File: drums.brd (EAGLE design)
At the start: 212.1 x 294.3 mm, 210 parts, among them IC1 4051N, IC3 7812T, IC5 OPA2134P, IC6 OPA4130P, IC7 LM2574HVN-5.0, IC8 74LS595N, J2 UBBS-4R-D14-4D

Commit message: added hihats, buncha stuff
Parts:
- added C49, C52, C56, C57, C64, C65: 15n, dan:C050-025X075
- added C50, C51: 10n, dan:C050-025X075
- added C53, C54: 12n, dan:C050-025X075
- added C55: 3.3n, dan:C050-025X075
- added C58, C62: 1u, dan:E2-5
- added C59: np, dan:C050-025X075
- added C60: .47u, dan:E2-5
- added C61: 5.6n, dan:C050-025X075
- added C63: np, dan:E2-5
- added C66: 33u, dan:E2-5
- added CHDECAY: 50k, dan:EVUFXJ
- added D13, D14, D15, D16: 1N4148DO35-7, dan:DO35-7
- added HATFILTER, VOLUME: 10k, dan:EVUFXJ
- added HATSLEVEL, OHDECAY1: 500k, dan:EVUFXJ
- added IC2: 4584N, dan:DIL14
- added IC9: OPA4130P, dan:DIL14
- added JP7, JP8: (no value), dan:2X06
- added R101, R102, R103, R104, R105, R24: 150k, dan:0207/2V
- added R106: 1k, dan:0207/2V
- added R107, R131, R132, R133: 33k, dan:0207/2V
- added R108, R109: 100, dan:0207/2V
- added R110: 1M, dan:0207/2V
- added R111, R115, R123, R127: 22k, dan:0207/2V
- added R112, R130: 220, dan:0207/2V
- added R113, R118, R121, R126: 4.7k, dan:0207/2V
- added R114, R116, R117, R120, R122, R124, R125: 10k, dan:0207/2V
- added R119, R16, R20: 330k, dan:0207/2V
- added R128, R129, R134, R135, R136: 100k, dan:0207/2V
- added R137: 82k, dan:0207/2V
- added R19, R21: 470k, dan:0207/2V
- added R22, R23: 560k, dan:0207/2V
- added U$14, U$16, U$18, U$19, U$20, U$21, U$22: 2N3904_, dan:TO92-EBC
- added U$15, U$17: 2N3906_, dan:TO92-EBC
- moved R2 212.5 mm to (76.2, 242.6)
- moved U$8 54.6 mm to (81.3, 87.6), flipped to the top
- moved R96 48.7 mm to (53.3, 71.1), flipped to the bottom
- moved MENU1 47.3 mm to (49.5, 61.0)
- moved C47 47.3 mm to (49.5, 73.7), flipped to the bottom
- moved R95 47.1 mm to (45.7, 71.1), flipped to the bottom
- moved R25 42.6 mm to (184.2, 62.2), flipped to the top
- moved C7 42.6 mm to (181.6, 52.1)
- moved C21 33.8 mm to (177.8, 132.1), turned to 180 degrees
- moved D+ 31.8 mm to (24.1, 78.7), turned to 270 degrees
- moved D- 30.0 mm to (26.7, 78.7), turned to 270 degrees
- moved C44 24.1 mm to (33.0, 134.6), turned to 90 degrees
- moved JP1 21.6 mm to (5.08, 76.2)
- moved C9 20.7 mm to (31.8, 252.7), turned to 180 degrees
- moved IC8 20.4 mm to (44.5, 85.1), turned to 180 degrees
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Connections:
- removed net N$132: JP1.6
- removed net N$138: JP2.4
- removed net N$144: JP2.3
- removed net N$145: JP2.5
- removed net N$2: R2.2, U$1.3.3V
- removed net N$32: JP1.3
- removed net N$35: R18.1, U$1.1
- removed net N$48: JP1.11
- removed net N$50: JP1.4
- removed net VCC: IC1.16, IC8.16
- removed net VEE: IC1.7
- new net CHDEC2A: CHDECAY.3
- new net CHDEC2B: C64.1, D13.A, JP2.5
- new net CHDEC3B: C60.+, D14.C, JP2.6
- new net CHDECA: CHDECAY.1, CHDECAY.2, JP1.4, JP1.6
- new net CHDECB: JP2.4, R119.2
- new net D+B: J2.D+, JP2.10
- new net D-B: J2.D-, JP2.11
- new net HATLEV2A: HATSLEVEL.1, JP1.9
- new net HATLEV2B: C66.-, JP2.9
- new net HATLEVA: HATSLEVEL.2, HATSLEVEL.3, JP1.8
- new net HATLEVB: IC9.7, JP2.8, R134.1
- new net HFILTA: HATFILTER.3, JP1.3
- new net HFILTB: JP2.3, R108.2
- new net MIDRXA: JP1.12, U$1.0
- new net MIDRXB: JP2.12, OK1.6, R2.1
- new net MIDTXA: JP1.5, U$1.1
- new net MIDTXB: JP2.7, R18.1
- new net N$106: IC2.12, R105.2, R23.1
- new net N$107: C54.1, IC2.13, R23.2
- new net N$109: C58.+, R110.2, U$14.B
- new net N$110: C55.2, R101.1, R102.1, R103.1, R104.1, R105.1, R106.1, R24.1
- new net N$143: C55.1, R107.2
- new net N$149: C56.2, IC9.2, R107.1, R137.2
- new net N$150: C56.1, C57.2, R108.1
- new net N$151: C57.1, C58.-, IC9.1, R137.1
- new net N$152: R109.1, U$14.C
- new net N$155: C59.1, D13.C, D15.C, U$14.E
- new net N$156: JP8.12
- new net N$158: D14.A, R112.1
- new net N$159: R113.1, R114.2, U$15.B
- new net N$161: R111.2, R112.2, U$15.E
- new net N$162: R113.2, R117.1, R118.1, U$15.C
- new net N$163: R114.1, U$16.E
- new net N$164: R115.1, R116.1, U$16.B
- new net N$168: D16.A, R127.2, U$17.E
- new net N$169: R121.1, R122.2, U$17.B
- new net N$170: R121.2, R125.1, R126.1, U$17.C
- new net N$171: R122.1, U$18.E
- new net N$173: R123.1, R124.1, U$18.B
- new net N$176: R120.2, R127.1, U$19.B
- new net N$177: C61.1, R128.2, U$19.E
- new net N$178: C65.1, D15.A, R133.1
- new net N$179: R128.1, U$20.B
- new net N$180: C63.+, R129.2, U$20.E, U$21.E
- new net N$181: D16.C, R130.2
- new net N$183: R131.1, U$22.B
- new net N$184: R132.2, R133.2, U$22.C
- new net N$185: R119.1, U$21.B
- new net N$187: C64.2, R136.2
- new net N$188: C65.2, R135.2
- new net N$189: C66.+, IC9.6, R134.2, R135.1, R136.1
- new net N$31: C52.1, IC2.9, R21.2
- new net N$49: IC2.8, R103.2, R21.1
- new net N$67: IC2.2, R16.1, R24.2
- new net N$71: C49.1, IC2.1, R16.2
- new net N$74: C50.1, IC2.3, R19.2
- new net N$75: IC2.4, R101.2, R19.1
- new net N$79: IC2.6, R102.2, R20.1
- new net N$80: C51.1, IC2.5, R20.2
- new net N$85: C53.1, IC2.11, R22.2
- new net N$86: IC2.10, R104.2, R22.1
- new net OHDECA: JP7.2, OHDECAY1.1
- new net OHDECB: C62.+, JP8.2, R129.1, R130.1, R131.2
- new net T5B: JP8.3, R115.2
- new net T6B: JP8.4, R123.2
- new net T7B: JP8.5, R118.2, R126.2
- net +12V: now also IC9.4, R110.1, R117.2, R125.2, U$22.E
- net -12V: now also IC9.11
- net 3.3V: now also IC1.16, IC2.14, U$1.3.3V; no longer OK1.6, R2.1, U$1.0
- net 5V: now also IC8.16, R2.2
- net D+A: now also JP1.10; no longer J2.D+
- net D-A: now also JP1.11; no longer J2.D-
- net GND: now also C49.2, C50.2, C51.2, C52.2, C53.2, C54.2, C59.2, C60.-, C61.2, C62.-, C63.-, HATFILTER.1, HATFILTER.2, IC1.7, IC2.7, IC9.3, IC9.5, JP1.7, JP7.1, JP8.1, OHDECAY1.2, OHDECAY1.3, R106.2, R109.2, R111.1, R116.2, R120.1, R124.2, R132.1, U$16.C, U$18.C, U$19.C, U$20.C, U$21.C
- net N$134: now also JP8.7; no longer JP1.8
- net N$135: now also JP8.9; no longer JP1.10
- net N$136: now also JP8.11; no longer JP1.12
- net N$139: now also JP7.6; no longer JP2.6
- net N$140: now also JP7.8; no longer JP2.8
- net N$141: now also JP7.10; no longer JP2.10
- net N$142: now also JP7.12; no longer JP2.12
- net N$146: now also JP8.6; no longer JP2.7
- net N$147: now also JP8.8; no longer JP2.9
- net N$148: now also JP8.10; no longer JP2.11
- net N$38: now also JP7.7; no longer JP1.5
- net N$39: now also JP7.9; no longer JP1.7
- net N$47: now also JP7.11; no longer JP1.9
- net T5: now also JP7.3
- net T6: now also JP7.4
- net T7: now also JP7.5
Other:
- board size 212.1 x 294.3 mm -> 212.1 x 276.5 mm

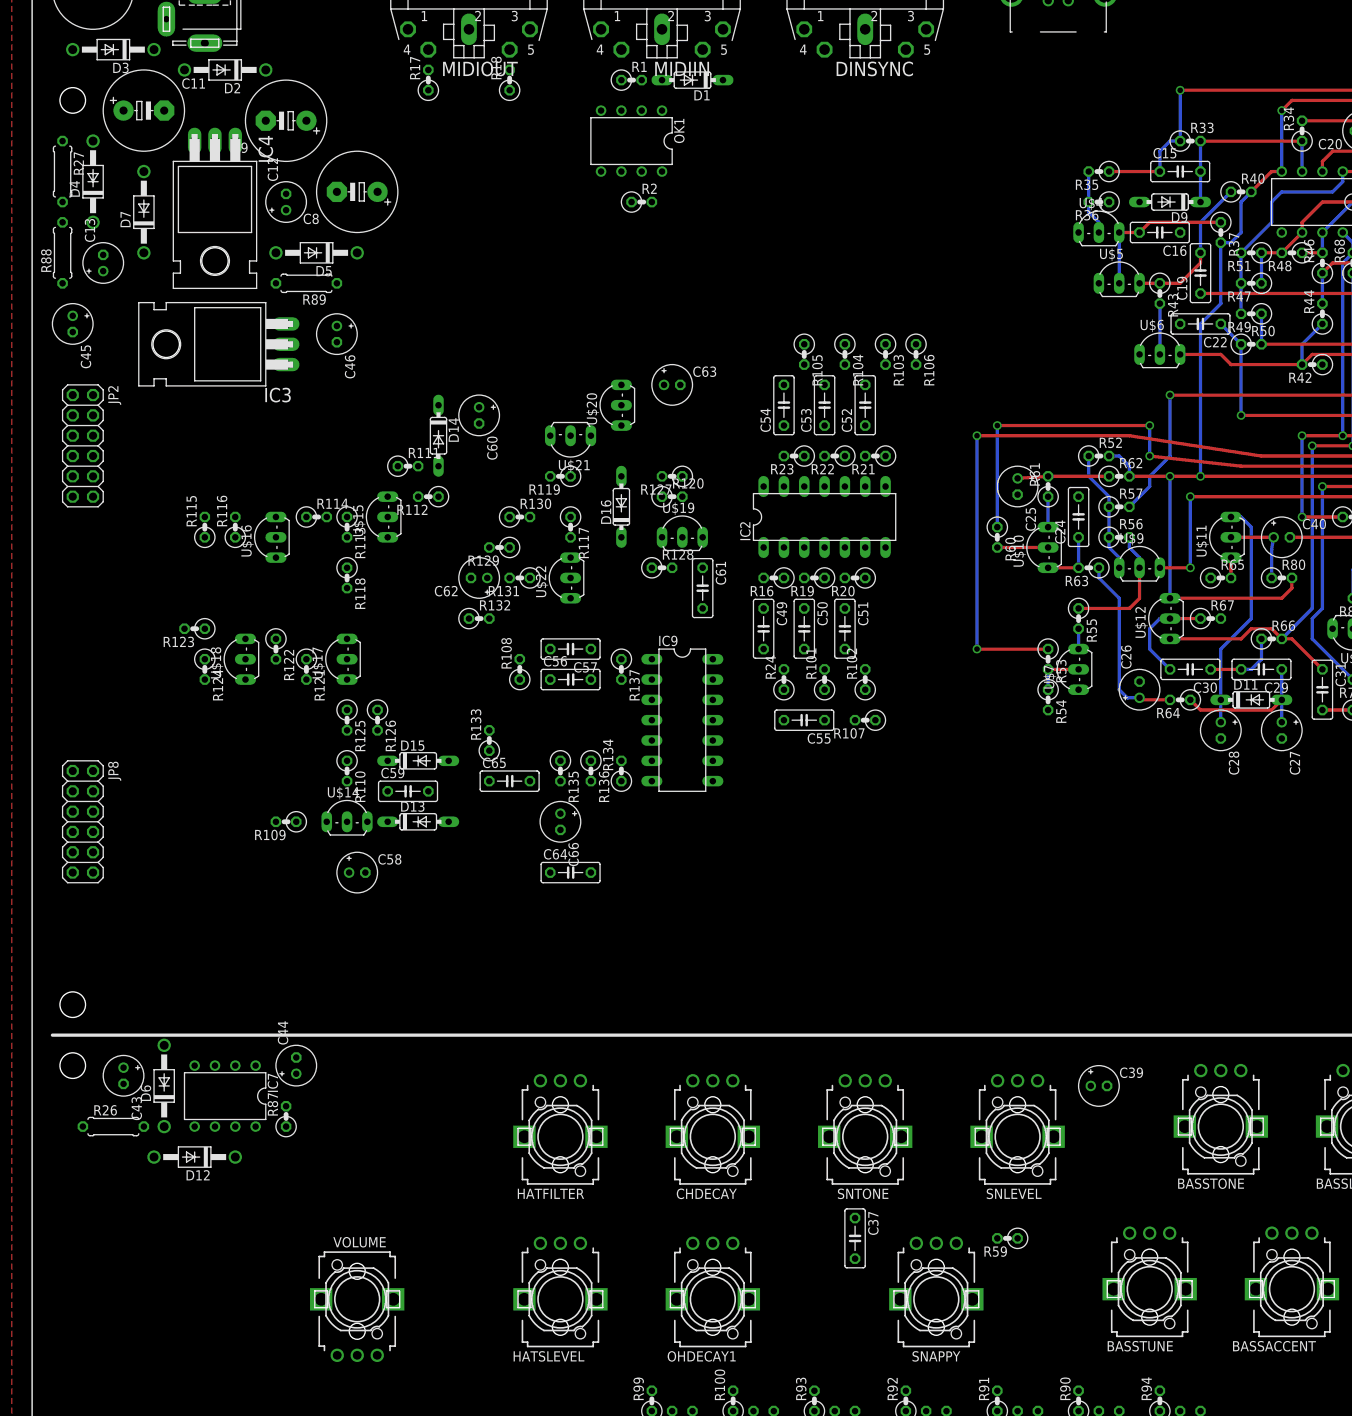
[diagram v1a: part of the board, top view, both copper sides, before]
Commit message: made hihat layout
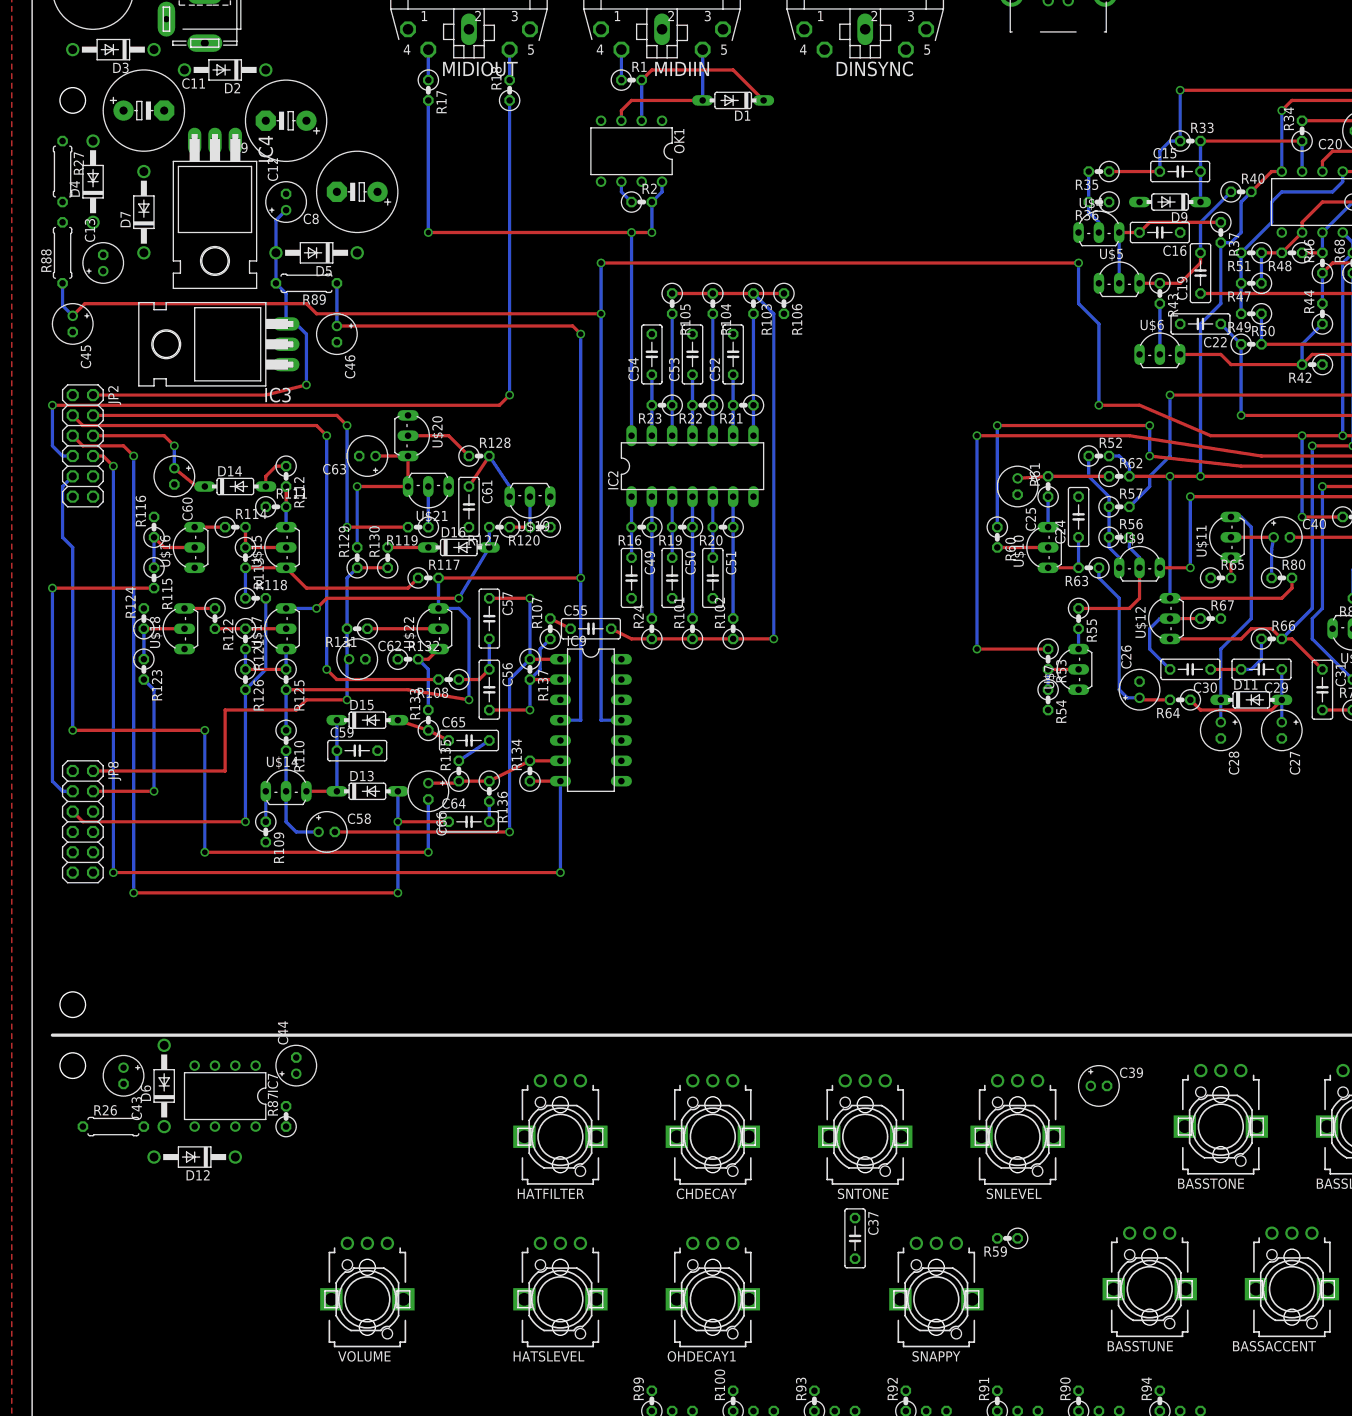
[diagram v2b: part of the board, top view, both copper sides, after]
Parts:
- moved R107 41.0 mm to (64.8, 189.2), turned to 90 degrees
- moved C63 39.1 mm to (41.9, 210.8), turned to 180 degrees
- moved C60 38.9 mm to (17.8, 208.3)
- moved C61 30.9 mm to (54.6, 204.5)
- moved C55 29.0 mm to (69.8, 189.2), turned to 0 degrees
- moved R128 26.8 mm to (55.9, 210.8)
- moved D14 26.2 mm to (25.4, 207.0), turned to 0 degrees
- moved U$20 24.4 mm to (48.3, 213.4), turned to 270 degrees
- moved R127 22.5 mm to (58.4, 201.9)
- moved R131 21.3 mm to (40.6, 189.2)
- moved D16 20.9 mm to (53.3, 199.4), turned to 0 degrees
- moved U$19 19.2 mm to (62.2, 204.5), turned to 180 degrees
- moved R119 18.9 mm to (48.3, 201.9)
- moved R117 18.9 mm to (49.5, 195.6), turned to 0 degrees
- moved U$21 18.9 mm to (49.5, 205.7)
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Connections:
- removed net N$36: DINSYNC.1, U$1.10
- removed net N$37: DINSYNC.3, U$1.11
- new net DINCLA: U$1.11
- new net DINCLB: DINSYNC.3
- new net DINSTA: U$1.10
- new net DINSTB: DINSYNC.1
- net 3.3V: now also IC8.16; no longer IC2.14, R17.2
- net 5V: now also IC2.14, R17.2; no longer IC8.16
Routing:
- net -12V: track 153.8 -> 389.9 mm, vias 8 -> 12
- net +12V: track 213.5 -> 364.7 mm, vias 5 -> 8
- net HATLEVB: track 0.00 -> 125.0 mm, vias 0 -> 3
- net CHDEC2B: track 0.00 -> 115.4 mm, vias 0 -> 4
- net MIDTXB: track 0.00 -> 102.7 mm, vias 0 -> 2
- net HATLEV2B: track 0.00 -> 99.1 mm, vias 0 -> 4
- net N$110: track 0.00 -> 78.8 mm, vias 0 -> 1
- net 5V: track 0.00 -> 76.7 mm, vias 0 -> 3
- net HFILTB: track 0.00 -> 76.5 mm, vias 0 -> 2
- net N$151: track 0.00 -> 61.0 mm, vias 0 -> 2
- net OHDECB: track 0.00 -> 61.0 mm, vias 0 -> 1
- net CHDECB: track 0.00 -> 52.6 mm, vias 0 -> 2
- net 12V: track 0.00 -> 51.5 mm, vias 0 -> 1
- net T7B: track 0.00 -> 51.1 mm, vias 0 -> 1
- net T5B: track 0.00 -> 39.9 mm, vias 0 -> 1
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
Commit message: added toms
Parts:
- added C67, C85: 33u, dan:E2-5
- added C68: 4.7n, dan:C050-025X075
- added C69, C70: 27n, dan:C050-025X075
- added C71, C78: 47u, dan:E2-5
- added C72: .47u, dan:C050-025X075
- added C73: 3.9n, dan:C050-025X075
- added C74, C75, C81: 18n, dan:C050-025X075
- added C76: 68n, dan:C050-025X075
- added C77, C79: 47n, dan:C050-025X075
- added C80: 39n, dan:C050-025X075
- added C82: 10n, dan:C050-025X075
- added C83, C84: 1u, dan:E2-5
- added D17, D18: 1N4148DO35-7, dan:DO35-7
- added HATSLEVEL1: 500k, dan:EVUFXJ
- added HTOMTUN, LTOMTUN: 1k, dan:EVUFXJ
- added IC10: OPA2134P, dan:DIL08
- added LTOMDEC: 1M, dan:EVUFXJ
- added R138, R151, R153, R166, R178: 100k, dan:0207/2V
- added R139, R182, R183: 15k, dan:0207/2V
- added R140, R157: 1k, dan:0207/2V
- added R141, R158, R174, R176, R177, R179: 4.7k, dan:0207/2V
- added R142, R144, R145, R146, R147, R154, R159, R161, R162, R163, R164, R175, R180: 10k, dan:0207/2V
- added R143, R160, R181: 22k, dan:0207/2V
- added R148, R165, R184, R186: 47k, dan:0207/2V
- added R149, R167: 2.2M, dan:0207/2V
- added R150, R152, R168: 100, dan:0207/2V
- added R155, R169: 680k, dan:0207/2V
- added R156: 72k, dan:0207/2V
- added R170: 39k, dan:0207/2V
- added R171: 2.2k, dan:0207/2V
- added R172: 1M, dan:0207/2V
- added R173, R185: 33k, dan:0207/2V
- added TOMLEV: 10k, dan:EVUFXJ
- added U$23, U$27, U$28: 2N3906_, dan:TO92-EBC
- added U$24, U$25, U$26, U$29, U$30, U$31, U$32: 2N3904_, dan:TO92-EBC
- BASSTONE: value US-EVUF2J -> 10k
- BASSTUNE: value US-EVUF2J -> 250k
- moved VOLUME 166.3 mm to (198.1, 48.3)
- moved LED2 76.7 mm to (193.0, 125.7)
- moved R91 75.1 mm to (191.8, 116.8), turned to 270 degrees
- moved LED4 61.3 mm to (152.4, 125.7)
- moved R93 59.1 mm to (151.1, 118.1), turned to 270 degrees
- moved LED1 52.2 mm to (174.0, 125.7)
- moved R90 48.4 mm to (172.7, 116.8)
- moved LED5 46.7 mm to (111.8, 124.5)
- moved LED3 40.5 mm to (134.6, 125.7)
- moved LED7 38.8 mm to (71.1, 124.5)
- moved R94 38.1 mm to (110.5, 115.6), turned to 270 degrees
- moved HATFILTER 37.7 mm to (92.7, 99.1)
- moved R92 35.0 mm to (133.3, 118.1), turned to 270 degrees
- moved C44 34.7 mm to (16.5, 104.1), turned to 270 degrees
- moved LED6 34.5 mm to (91.4, 124.5)
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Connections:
- net N$147 renamed T8B
- net N$148 renamed T10B
- removed net N$135: JP8.9
- removed net N$139: JP7.6
- removed net N$140: JP7.8
- removed net N$141: JP7.10
- removed net N$39: JP7.9
- removed net T5B: JP8.3, R115.2
- new net CHATLEV2A: HATSLEVEL1.1, JP7.7
- new net CHATLEV2B: C67.-, JP8.7
- new net CHATLEVA: HATSLEVEL1.2, HATSLEVEL1.3, JP7.6
- new net CHATLEVB: IC9.8, JP8.6, R138.1
- new net HTOMTUNA: HTOMTUN.2, HTOMTUN.3
- new net HTOMTUNB: R168.2, U$30.E
- new net LTOMDEC2A: LTOMDEC.3
- new net LTOMDEC2B: C85.+
- new net LTOMDECA: LTOMDEC.1, LTOMDEC.2
- new net LTOMDECB: IC10.1, R184.1, R186.2
- new net LTOMTUNA: LTOMTUN.2, LTOMTUN.3
- new net LTOMTUNB: R150.2, U$25.E
- new net N$132: C68.2, IC9.12, R148.2
- new net N$137: C70.2, IC9.14, R149.1, R183.1, R185.2
- new net N$138: C69.2, C70.1, R150.1, R186.1
- new net N$144: C71.+, R152.2, R153.1, U$27.C
- new net N$145: C76.1, R171.1, R172.2
- new net N$157: C72.1, R155.2, R169.1, U$27.E
- new net N$165: R154.2, U$27.B
- new net N$167: R155.1, R156.2, U$25.B
- new net N$174: C77.2, R172.1, R173.2
- new net N$175: D18.A, R164.2, R166.2, U$28.E
- new net N$182: R158.1, R159.2, U$28.B
- new net N$186: R158.2, R162.1, R163.1, U$28.C
- new net N$190: R159.1, U$29.E
- new net N$191: R160.1, R161.1, U$29.B
- new net N$192: C73.1, R157.2, R164.1
- new net N$193: C73.2, IC10.5, R165.2
- new net N$194: R151.1, R166.1, U$26.B
- new net N$195: D17.C, D18.C, R171.2
- new net N$196: R173.1, U$31.B
- new net N$197: C74.1, IC10.6, R167.2
- new net N$198: C75.2, IC10.7, R167.1, R182.1
- new net N$199: C74.2, C75.1, R168.1
- new net N$2: C67.+, IC9.9, R136.1, R138.2
- new net N$201: R169.2, R170.2, U$30.B
- new net N$202: C79.1, R174.2, U$31.E
- new net N$203: C78.+, R174.1, R175.2
- new net N$204: C77.1, R179.1, R180.2
- new net N$205: C81.2, R181.1, U$32.B
- new net N$206: C79.2, R176.1, R177.1
- new net N$207: C80.1, U$32.C
- new net N$208: C82.2, R177.2, R178.1
- new net N$209: C85.-, IC10.2, R184.2, R185.1
- new net N$210: C84.+, R182.2
- new net N$211: C83.+, R183.2
- new net N$215: TOMLEV.2
- new net N$216: U$1.23/A9
- new net N$218: U$1.22/A8
- new net N$32: R139.1
- new net N$35: D17.A, R147.2, R151.2, U$23.E
- new net N$36: R141.1, R142.2, U$23.B
- new net N$37: R141.2, R145.1, R146.1, U$23.C
- new net N$48: R143.1, R144.1, U$24.B
- new net N$50: C68.1, R140.2, R147.1
- new net T10: JP7.10, U$1.21/A7
- new net T9: JP7.9, U$1.20/A6
- new net T9B: JP8.3, JP8.9, R115.2, R143.2, R160.2
- new net TOMSLEVA: TOMLEV.1
- new net TOMSLEVB: C83.-, C84.-, R178.2
- net +12V: now also IC10.4, R145.2, R152.1, R162.2, R175.1, U$32.E
- net -12V: now also IC10.8
- net GND: now also C71.-, C72.2, C76.2, C78.-, C81.1, C82.1, HTOMTUN.1, IC10.3, IC9.10, LTOMTUN.1, R140.1, R144.2, R148.1, R156.1, R157.1, R161.2, R165.1, R170.1, R176.2, R179.2, TOMLEV.3, U$24.C, U$25.C, U$26.C, U$29.C, U$30.C, U$31.C
- net N$134: now also C69.1, IC9.13, R149.2; no longer JP8.7
- net N$146: now also R153.2, R154.1, U$26.E; no longer JP8.6
- net N$177: now also R139.2
- net N$189: no longer R136.1
- net N$38: now also R142.1, U$24.E; no longer JP7.7
- net T7B: now also R146.2, R163.2
- net T8: now also JP7.8
- net WNOISE: now also C80.2, R180.1, R181.2
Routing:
- net CHDEC2B: track 115.4 -> 63.3 mm, vias 4 -> 2
- net T9B: track 0.00 -> 39.9 mm, vias 0 -> 1
- net T5B: track 39.9 -> 0.00 mm, vias 1 -> 0
- net T2B: track 131.0 -> 116.8 mm, vias 4 -> 3
- net N$177: track 10.4 -> 23.9 mm, vias 0 -> 1
- net N$2: track 0.00 -> 7.62 mm
- net CHATLEVB: track 0.00 -> 3.81 mm
- net N$179: track 8.67 -> 5.08 mm
- net N$110: track 78.8 -> 76.0 mm
- net HATLEVB: track 125.0 -> 122.4 mm
- net HATLEV2B: track 99.1 -> 96.6 mm
- net N$168: track 32.1 -> 34.1 mm
- net N$188: track 4.58 -> 6.35 mm
- net SNAP2B: track 100.4 -> 99.1 mm
- net N$79: track 15.2 -> 14.0 mm
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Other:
- board size 212.1 x 276.5 mm -> 212.1 x 268.9 mm
